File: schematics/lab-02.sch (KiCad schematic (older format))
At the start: 26 parts, among them U1 LM741, U2 LM741

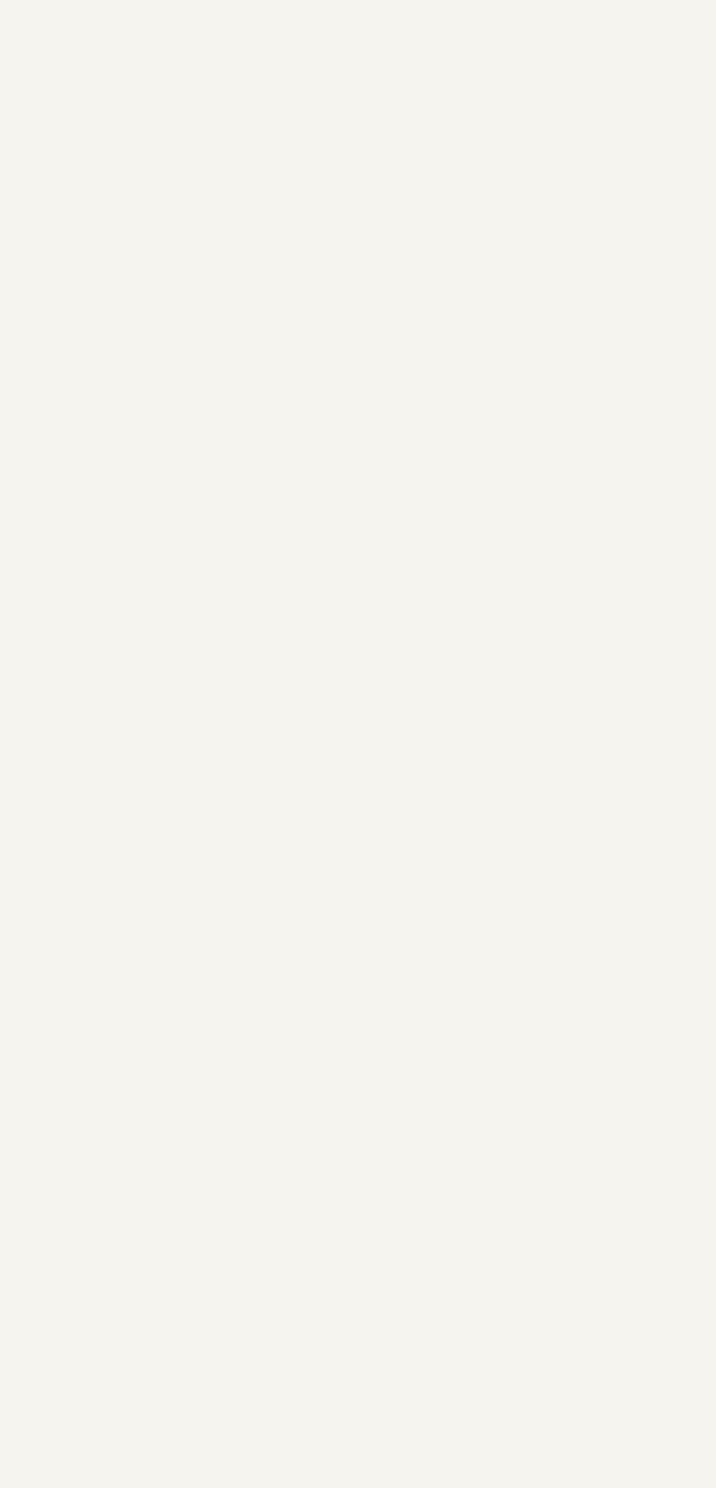
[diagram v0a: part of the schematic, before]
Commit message: Add low pass filter and clipper to schematics.
Update kicad source files and renders.
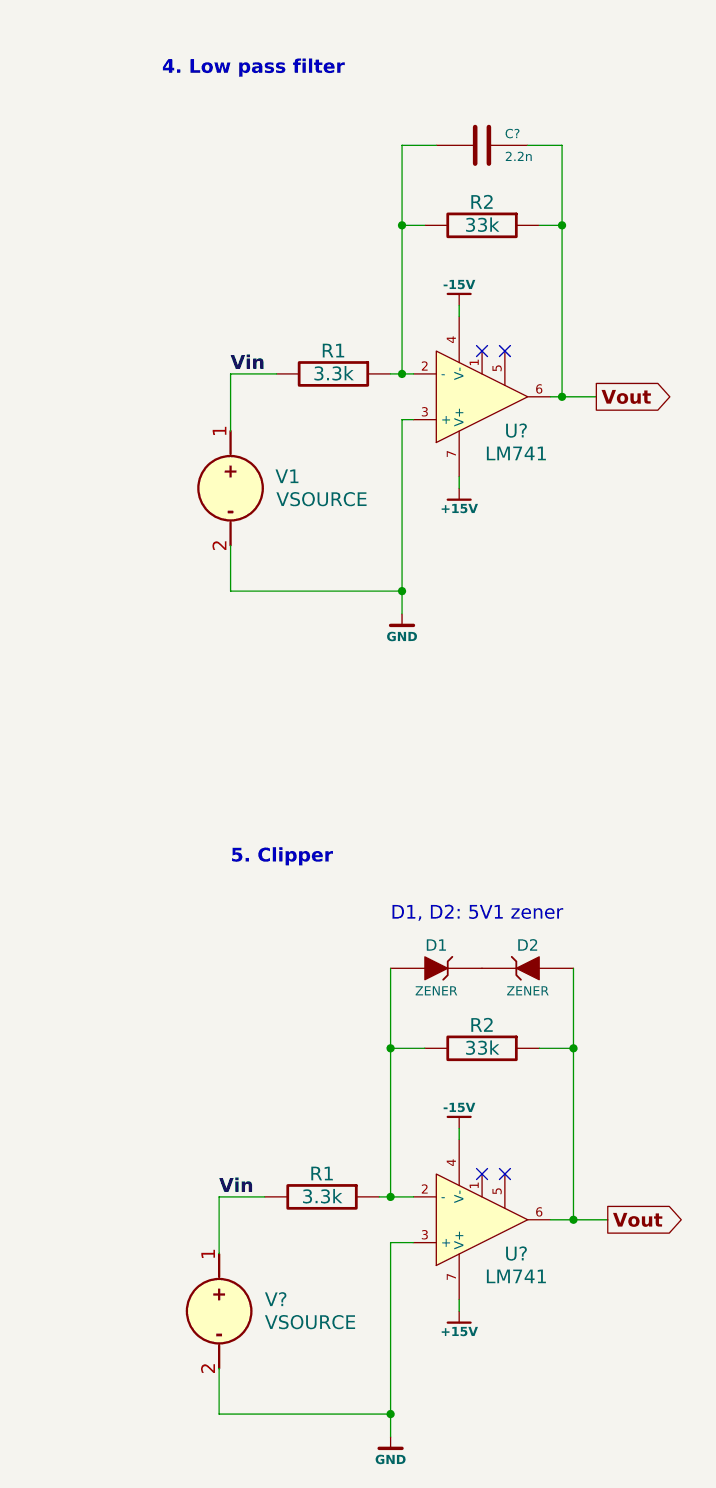
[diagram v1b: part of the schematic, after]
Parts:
- added C?: 2.2n, symbol C
- added D1, D2: ZENER, symbol ZENER
- added R1 (x2): 3.3k, symbol R
- added R2 (x2): 33k, symbol R
- added U? (x2): LM741, symbol LM741
- added V1, V?: VSOURCE, symbol VSOURCE
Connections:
- net +15V: now also U?.7 (V+), U?.7 (V+)
- net -15V: now also U?.4 (V-), U?.4 (V-)
- net GND: now also U?.3 (+), U?.3 (+), V1.2, V?.2
- net Vin: now also R1.2, R1.2, V1.1, V?.1
- net Vout: now also C?.1, D2.1 (A), R2.1, R2.1, U?.6, U?.6
- new net: C?.2, R1.1, R2.2, U?.2 (-)
- new net: D1.1 (A), R1.1, R2.2, U?.2 (-)
- new net: D1.2 (K), D2.2 (K)
- no-connect marks 12 -> 16
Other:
- note added: "4. Low pass filter"
- note added: "5. Clipper"
- note added: "D1, D2: 5V1 zener"
